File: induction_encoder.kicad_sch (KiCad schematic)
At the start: 66 parts, among them J402 Conn_01x06, U1 MT9105ET, U10 IPS2200, U11 ADS1115IDGS, U12 ADS1115IDGS, U2 MT9105ET, U4 MT9105ET, U5 MT9105ET, U7 ADS1115IDGS, U8 MT9105ET

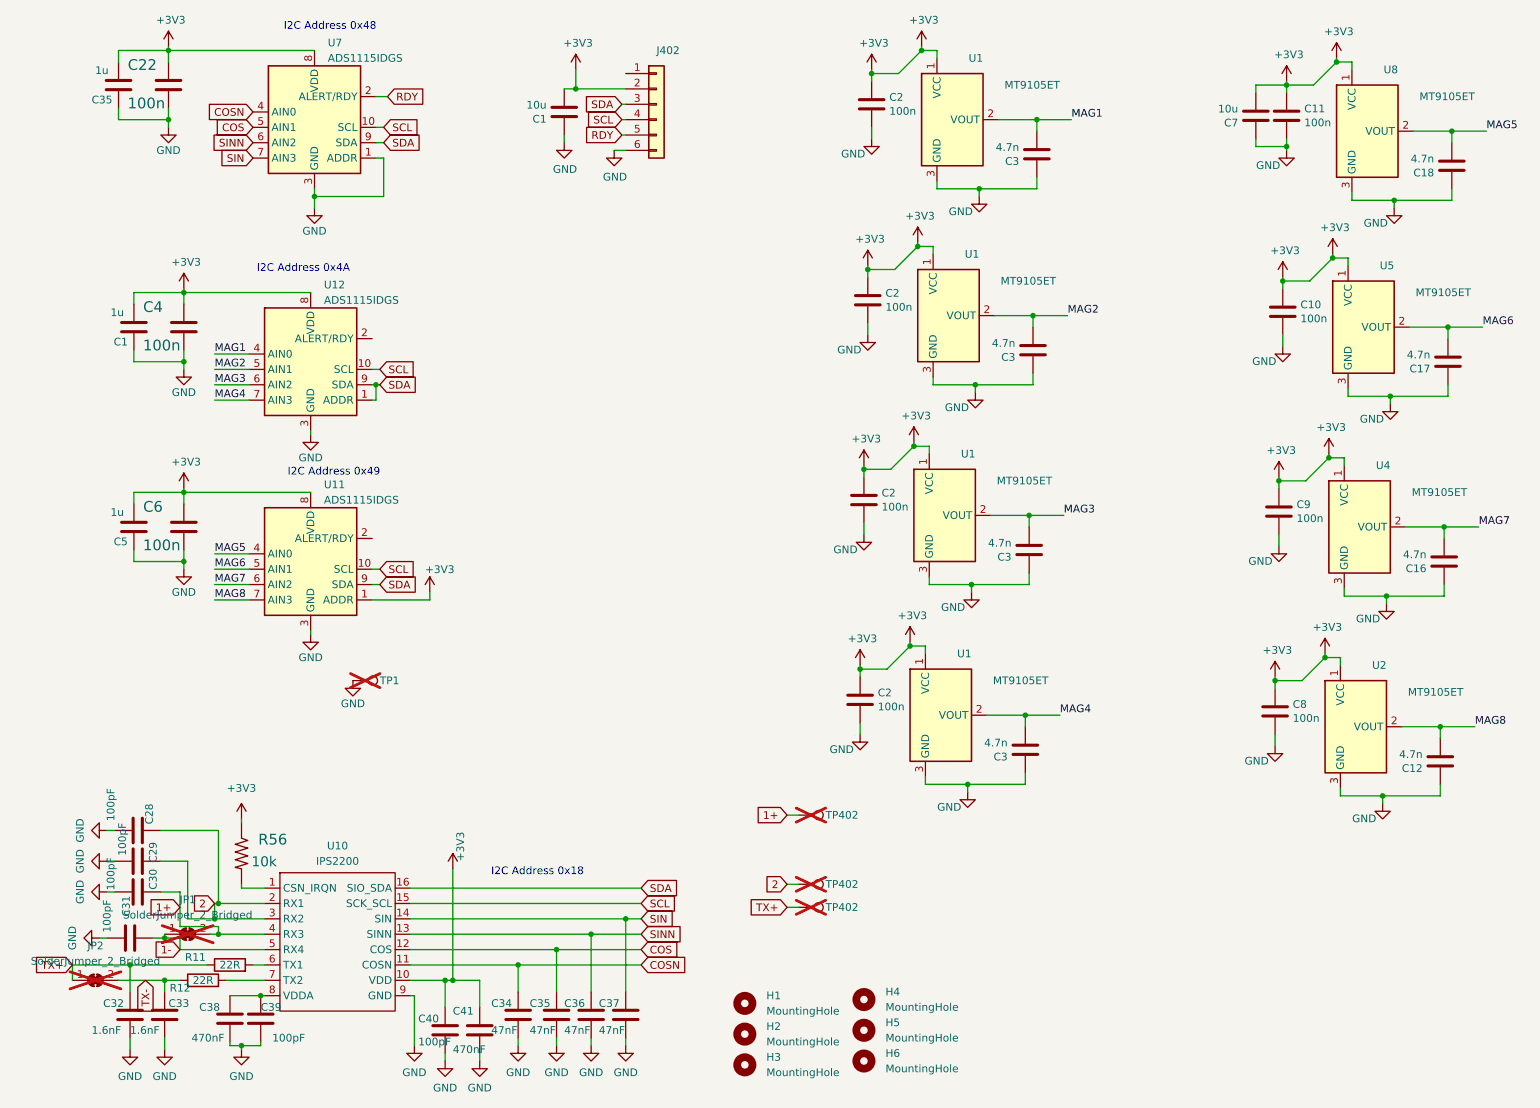
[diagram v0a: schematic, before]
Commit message: Update to rev 2, add I2C pullups and updated silk
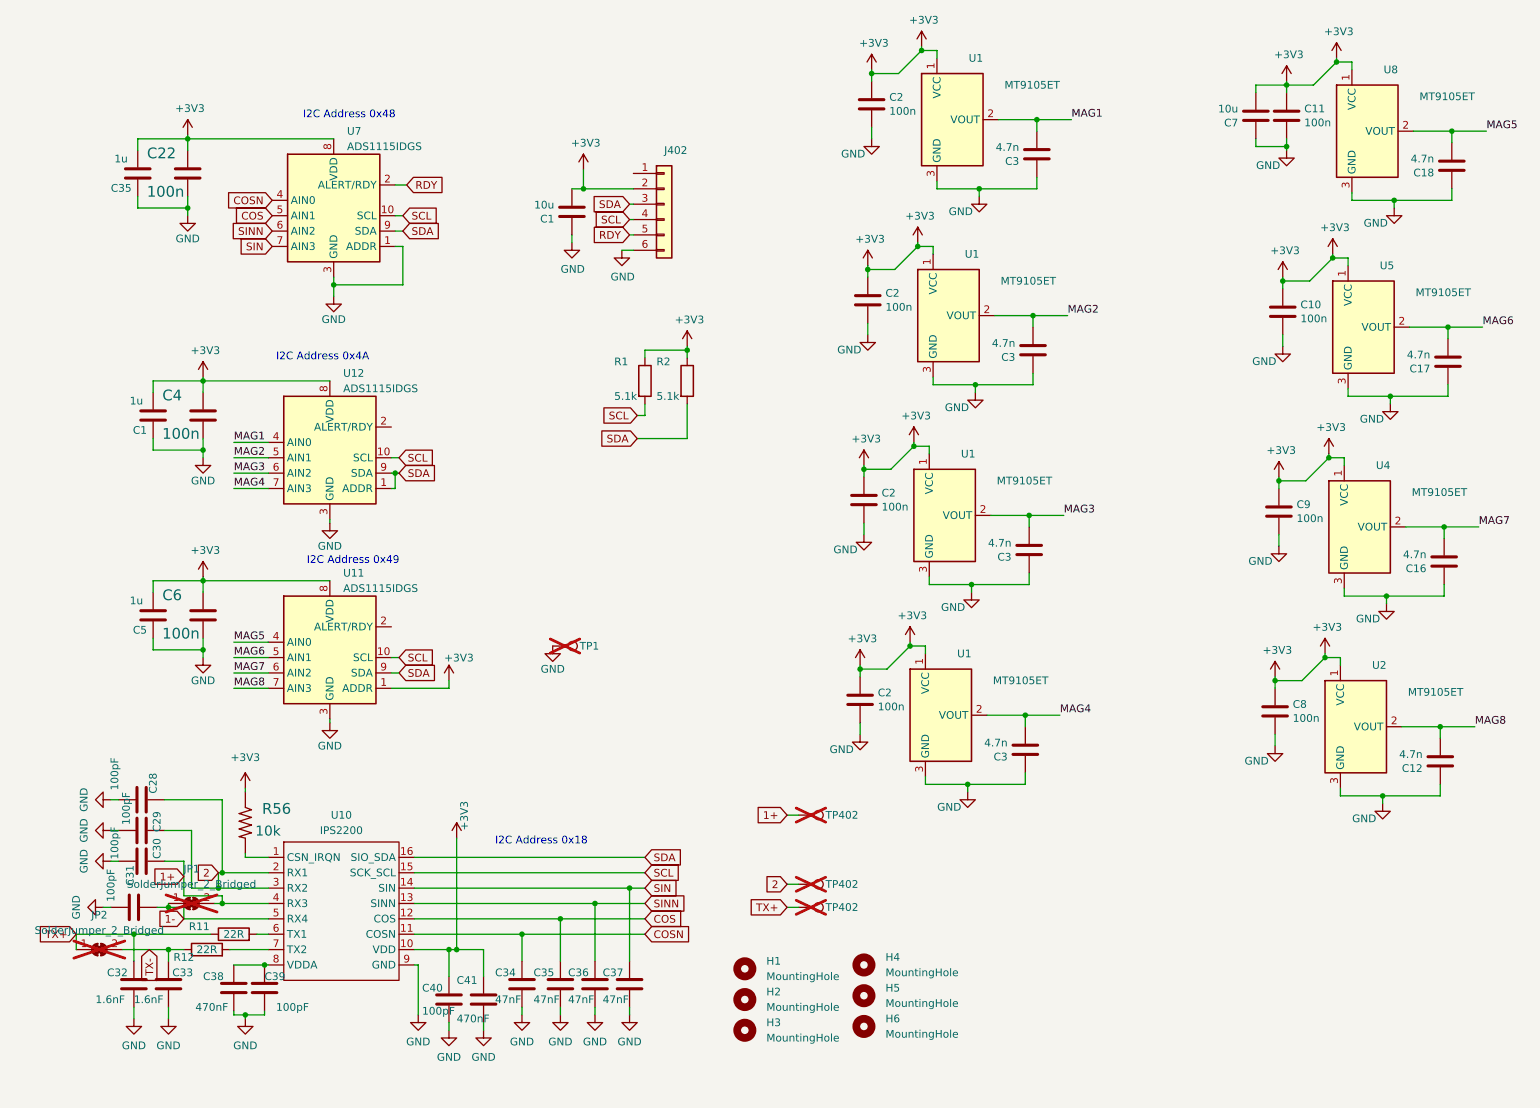
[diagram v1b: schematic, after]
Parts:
- added R1, R2: 5.1k, Resistor_SMD:R_0603_1608Metric, symbol Device:R
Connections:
- net +3V3: now also R1.1, R2.1
- net SCL: now also R1.2
- net SDA: now also R2.2
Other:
- moved on the sheet: C1, C22, C28, C29, C30, C31, C32, C33, C34, C35, C36, C37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

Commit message: Update induction encoder for order placed July 2024
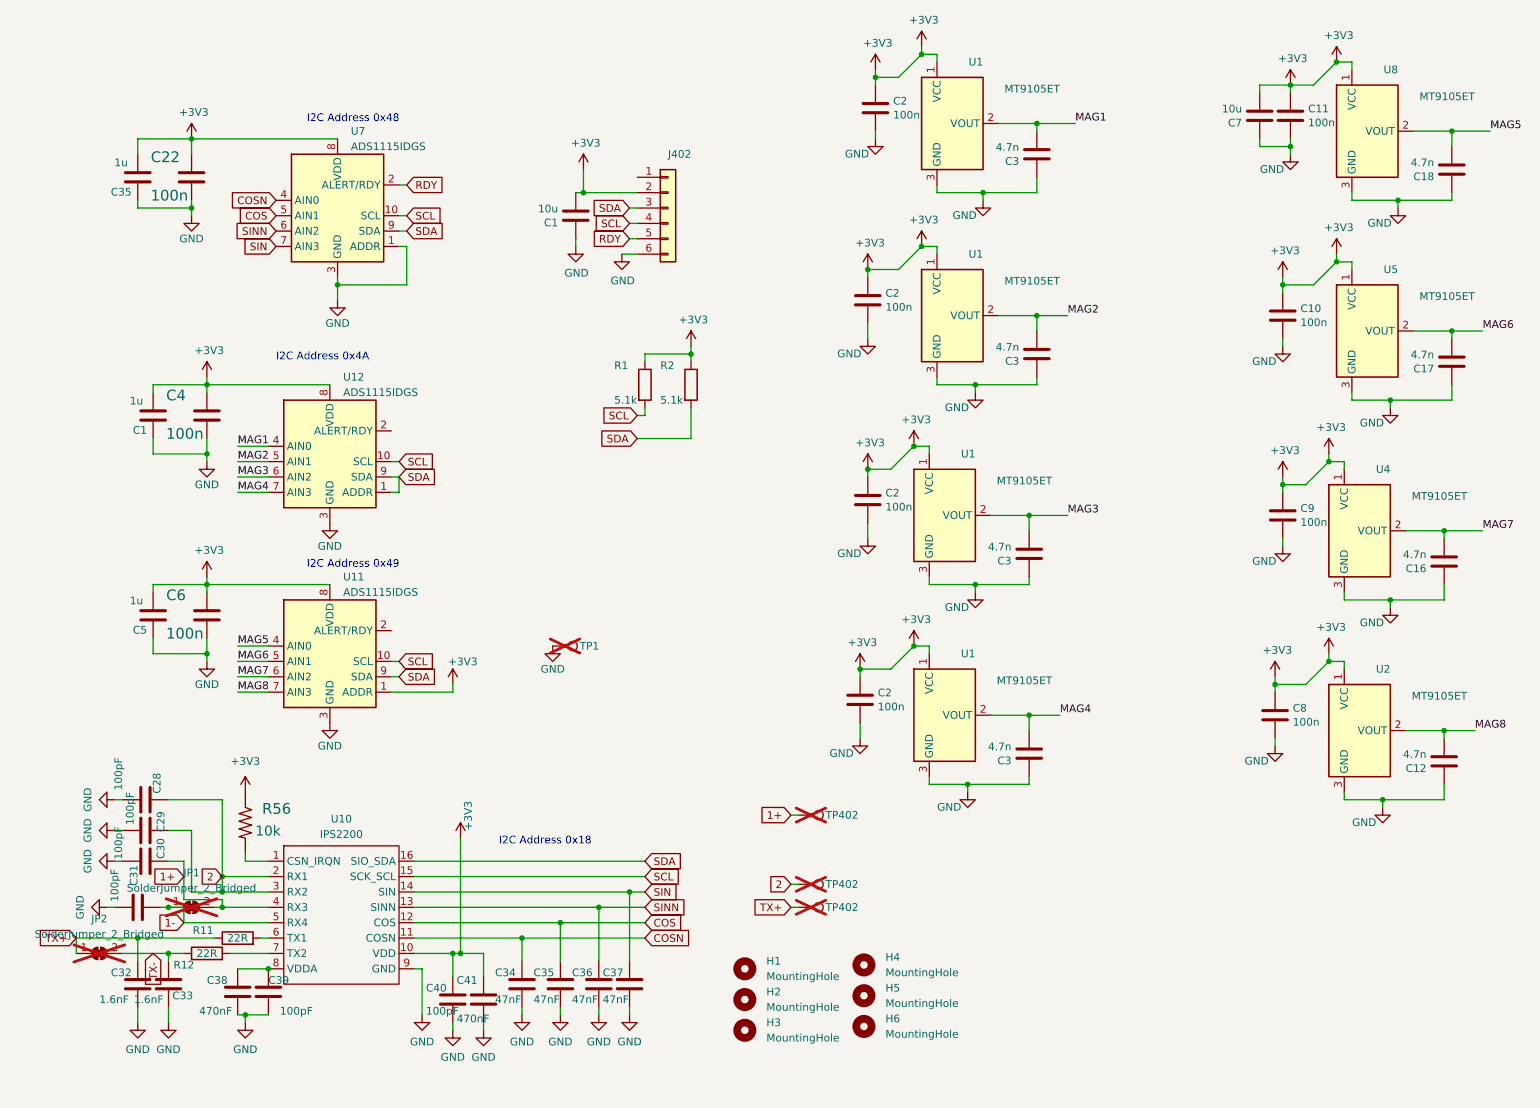
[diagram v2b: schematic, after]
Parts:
- R11, R12: LCSC C107701 -> C5139508
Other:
- moved on the sheet: C1, C10, C11, C12, C17, C18, C2, C22, C28, C29, C3, C30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
